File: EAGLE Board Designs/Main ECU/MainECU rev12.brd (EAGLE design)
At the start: 127 x 152.4 mm, 210 parts, among them J1 CONNECTOR-40__, J2 ADIS16460, J3 CONNECTOR-40__, J4 CONNECTOR-40__, J5 CONNECTOR-40__, K1 RELAY_DPDT_RT424024, K10 RELAY_DPDT_RT424024, K11 RELAY_DPDT_RT424024, K12 RELAY_DPDT_RT424024, K9 RELAY_DPDT_RT424024, Q3 TRANSISTOR_P_MOS_SOT-23_DMP30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, Q4 TRANSISTOR_N_MOS__DMG3406L-7, Q5 TRANSISTOR_P_MOS_SOT-23_DMP30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, Q6 TRANSISTOR_N_MOS__DMG3406L-7, U1 VOLTAGE_REGULATOR_SOT-223_3.3V, U2 TCAN1051HQV-Q1, U23 ADC128S022, U3 TCAN1051HQV-Q1, U32 ADC128S022, U33 TCAN1051HQV-Q1, U34 OPAMP_1_CHANNEL_OPA991, U37 OPAMP_1_CHANNEL_OPA991, U38 LOGICGATE_OR, U39 OPAMP_1_CHANNEL_OPA991, U4 TCAN1051HQV-Q1, U41 OPAMP_1_CHANNEL_OPA991, U42 LOGICGATE_AND_DCK3, U43 OPAMP_1_CHANNEL_OPA991, U44 LOGICGATE_NOR, U45 TCAN1051HQV-Q1, U46 TCAN1051HQV-Q1, U5 ADM8316WBX30, U6 ADC128S022, U7 ADC128S022

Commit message: ripup
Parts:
- moved A1 59.1 mm to (81.0, 175.5)
- moved C2 59.1 mm to (87.9, 176.3)
- moved C1 59.1 mm to (74.2, 174.5)
- moved TP2 59.1 mm to (83.6, 169.2)
- moved R65 50.7 mm to (-24.4, 40.9)
- moved U44 50.7 mm to (-24.4, 43.2)
- moved D37 50.7 mm to (-16.5, 40.4)
- moved D38 50.7 mm to (-20.6, 40.4)
- moved Q3 50.7 mm to (-12.4, 40.4)
- moved Q4 50.7 mm to (-20.6, 44.2)
- moved R64 50.7 mm to (-16.5, 43.2)
- moved R66 50.7 mm to (-16.5, 45.0)
- moved C26 47.3 mm to (60.5, 160.0)
- moved VR1 45.6 mm to (-14.5, 86.6)
- moved TP4 44.9 mm to (-14.0, 3.30)
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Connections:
- net +24V: no longer J1.15, J1.16
- net +5V: no longer J1.14
- net CANH_1: now also J1.16; no longer J1.12
- net CANH_2: now also J1.12; no longer J1.8
- net CANH_3: now also J1.8; no longer J1.4
- net CANL_1: now also J1.14; no longer J1.10
- net CANL_2: now also J1.10; no longer J1.6
- net CANL_3: now also J1.6; no longer J1.2
- net GND: now also J1.15, J1.4; no longer J1.1
- net SHDN_B: now also J1.1, J1.2
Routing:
- net +24V: track 250.0 -> 145.3 mm, vias 12 -> 8
- net BRAKE_HIGH: track 167.7 -> 75.3 mm, vias 2 -> 1
- net BRAKE_MISSING: track 55.5 -> 0.00 mm, vias 2 -> 0
- net CURRENT_HIGH: track 32.4 -> 1.02 mm, vias 3 -> 0
- net CURRENT: track 43.6 -> 16.0 mm
- net +5V: track 123.1 -> 98.1 mm, vias 23 -> 13
- net CURRENT_MISSING: track 17.2 -> 0.00 mm
- net BRAKE_1: track 34.9 -> 17.8 mm
- net BSPD_FAULT: track 12.9 -> 0.00 mm
- net CANH_3: track 168.7 -> 159.8 mm
- net CANH_2: track 203.2 -> 194.4 mm
- net CANL_3: track 166.0 -> 157.1 mm
- net CANH_1: track 191.1 -> 182.3 mm
- net CANL_1: track 188.2 -> 179.4 mm
- net CANL_2: track 200.2 -> 191.4 mm
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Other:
- board text added: "HyTech Racing 2023 Main ECU rev12 Designed by Mikhail Allen"
- board text removed: "HyTech Racing 2023 Main ECU rev11 Designed by Mikhail Allen"

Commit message: routing progress
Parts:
- moved TP2 42.2 mm to (74.4, 128.0)
- moved A1 42.0 mm to (70.6, 134.9)
- moved C1 38.8 mm to (63.8, 137.2), turned to 90 degrees
- moved C2 37.3 mm to (73.9, 141.7), turned to 0 degrees
- moved C26 36.0 mm to (64.5, 124.2)
- moved U$5 26.6 mm to (12.4, 125.2)
- moved BMS 21.0 mm to (46.7, 122.4)
- moved IMD 21.0 mm to (50.5, 122.4)
- moved LATCH 21.0 mm to (54.4, 122.4)
- moved R30 21.0 mm to (46.7, 120.4)
- moved R23 21.0 mm to (54.4, 120.4)
- moved R29 21.0 mm to (50.5, 120.4)
- moved D1 4.07 mm to (46.7, 141.0)
- moved D2 4.07 mm to (50.8, 141.0)
- moved D3 4.07 mm to (54.9, 141.0)
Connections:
- net +24V: now also J3.40
- net +5V: now also J3.38
- net CANH_1: now also J1.12; no longer J1.16
- net CANH_2: now also J1.8; no longer J1.12
- net CANH_3: now also J1.4; no longer J1.8
- net CANL_1: now also J1.10; no longer J1.14
- net CANL_2: now also J1.6; no longer J1.10
- net CANL_3: now also J1.2; no longer J1.6
- net GND: now also J1.1, J1.14; no longer J1.15, J1.4
- net SHDN_B: now also J1.15, J1.16; no longer J1.1, J1.2, J3.1, J3.2
- net SHDN_G: now also J3.1, J3.2; no longer J3.39, J3.40
- net STEERING_1_EXT: now also J1.25
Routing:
- net SHDN_B: track 260.1 -> 137.6 mm, vias 8 -> 7
- net STEERING_1_EXT: track 0.00 -> 108.5 mm
- net +3V3: track 475.9 -> 438.5 mm, vias 19 -> 17
- net !AD2_CS: track 97.0 -> 67.5 mm
- net +24V: track 145.3 -> 168.4 mm
- net BMS_OK: track 151.7 -> 128.8 mm, vias 3 -> 2
- net OKHS_IN: track 151.2 -> 129.1 mm
- net LATCH_BTN: track 64.9 -> 44.4 mm
- net GND: track 9.01 -> 0.00 mm, vias 39 -> 49
- net BRAKE_1: track 17.8 -> 9.07 mm
- net +5V: track 98.1 -> 104.8 mm
- net ECU_CLK: track 197.8 -> 191.4 mm
- net ECU_SDI: track 201.8 -> 195.7 mm
- net ECU_SDO: track 188.2 -> 182.9 mm
- net CANL_1: track 179.4 -> 176.1 mm
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
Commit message: routing
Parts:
- removed A: LED_0603_BLUE, HyTechDevices:0603-LED
- removed BRAKE: LED_0603_YELLOW, HyTechDevices:0603-LED
- added B_HI, B_MIS, C_HI, C_MIS: LED_0603_YELLOW, HyTechDevices:0603-LED
- added G: LED_0603_RED, HyTechDevices:0603-LED
- added R37, R54, R55: RESISTOR_0603_180, HyTechDevices:0603-RES
- B: value LED_0603_GREEN -> LED_0603_BLUE
- C: value LED_0603_YELLOW -> LED_0603_GREEN
- D: value LED_0603_ORANGE -> LED_0603_YELLOW
- E: value LED_0603_RED -> LED_0603_ORANGE
- R41, R59: value RESISTOR_0603_41.2K -> RESISTOR_0603_43K
- moved D8 148.6 mm to (109.0, 93.0), turned to 180 degrees
- moved R35 148.4 mm to (105.4, 93.0)
- moved R36 148.2 mm to (102.1, 93.0)
- moved TP3 68.6 mm to (-16.3, 115.3)
- moved C3 68.6 mm to (-22.4, 110.7)
- moved C4 68.6 mm to (-19.3, 102.6)
- moved U1 68.6 mm to (-17.5, 108.5)
- moved C93 50.5 mm to (26.4, 36.1)
- moved R60 50.5 mm to (26.4, 31.5)
- moved R61 50.5 mm to (26.4, 29.7)
- moved U37 50.5 mm to (26.4, 33.8)
- moved C92 50.3 mm to (22.1, 36.1)
- moved R59 50.3 mm to (22.1, 31.5)
- moved U34 50.3 mm to (22.1, 33.8)
- moved D43 47.8 mm to (98.6, 93.0), flipped to the top, turned to 180 degrees
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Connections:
- removed net SHDN_A: R24.1
- new net N$28: B_MIS.2, R37.2
- new net N$29: C_HI.2, R54.2
- new net N$30: C_MIS.2, R55.2
- new net TCU_RX6: A3.D25, J3.23
- new net TCU_RX7: A3.D28, J3.24
- new net TCU_TX6: A3.D24, J3.22
- new net TCU_TX7: A3.D29, J3.25
- net !STEERING_2_CS: now also A2.D9, J3.12; no longer A2.D10
- net BMS_OK: now also J3.34
- net BRAKELIGHT_EN: now also J3.9
- net BRAKE_MISSING: now also R37.1
- net CURRENT_HIGH: now also R54.1
- net CURRENT_MISSING: now also R55.1
- net ECU_CLK: now also J3.13
- net ECU_SDI: now also J3.14
- net ECU_SDO: now also J3.15
- net FL_INTERLOCK_SENSE_EXT: now also J3.30
- net FR_INTERLOCK_SENSE_EXT: now also J3.28
- net GND: now also B_HI.1, B_MIS.1, C_HI.1, C_MIS.1, G.1, J3.16, J3.17, J3.26, J3.27, J3.35, J3.36, J3.37, J3.39, J3.7, J3.8; no longer A.1, BRAKE.1
- net INERTIA_SENSE_EXT: now also J3.31
- net INVERTER_24V_EN: now also J3.10
- net INVERTER_EN: now also J3.11
- net N$13: now also G.2; no longer F.2
- net N$16: now also B.2; no longer A.2
- net N$17: now also C.2; no longer B.2
- net N$18: now also D.2; no longer C.2
- net N$19: now also E.2; no longer D.2
- net N$20: now also F.2; no longer E.2
- net N$56: now also B_HI.2; no longer BRAKE.2
- net OKHS_IN: now also J3.33
- net RL_INTERLOCK_SENSE_EXT: now also J3.32
- net RR_INTERLOCK_SENSE_EXT: now also J3.29
- net SHDN_B: now also R24.1; no longer R25.1
- net SHDN_C: now also R25.1; no longer R26.1
- net SHDN_D: now also R26.1; no longer R27.1
- net SHDN_E: now also R27.1; no longer R28.1
- net SHDN_F: now also R28.1; no longer R38.1
- net SHDN_F_READ: now also A2.D18
- net SHDN_G: now also R38.1
- net SHDN_G_READ: now also A2.D19
- net TCU_RX4: now also J3.21
- net TCU_RX5: now also J3.18
- net TCU_TX4: now also J3.20
- net TCU_TX5: now also J3.19
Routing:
- net +3V3: track 438.5 -> 237.1 mm, vias 17 -> 7
- net TCU_TX7: track 0.00 -> 104.1 mm
- net TCU_RX7: track 0.00 -> 100.4 mm
- net TCU_RX6: track 0.00 -> 96.5 mm
- net BSPD_OK: track 155.0 -> 59.8 mm, vias 2 -> 0
- net TCU_TX6: track 0.00 -> 93.8 mm
- net +24V: track 168.4 -> 259.5 mm, vias 8 -> 9
- net BRAKE_HIGH: track 75.3 -> 0.00 mm, vias 1 -> 0
- net SHDN_A: track 63.8 -> 0.00 mm, vias 7 -> 0
- net !STEERING_2_CS: track 0.00 -> 38.9 mm, vias 0 -> 1
- net SHDN_B: track 137.6 -> 173.6 mm, vias 7 -> 8
- net FR_INTERLOCK_SENSE: track 39.9 -> 5.41 mm, vias 1 -> 0
- net INERTIA_SENSE_EXT: track 0.70 -> 33.4 mm
- net SHDN_F_READ: track 38.1 -> 6.14 mm, vias 1 -> 0
- net RR_INTERLOCK_SENSE: track 37.0 -> 5.25 mm, vias 1 -> 0
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
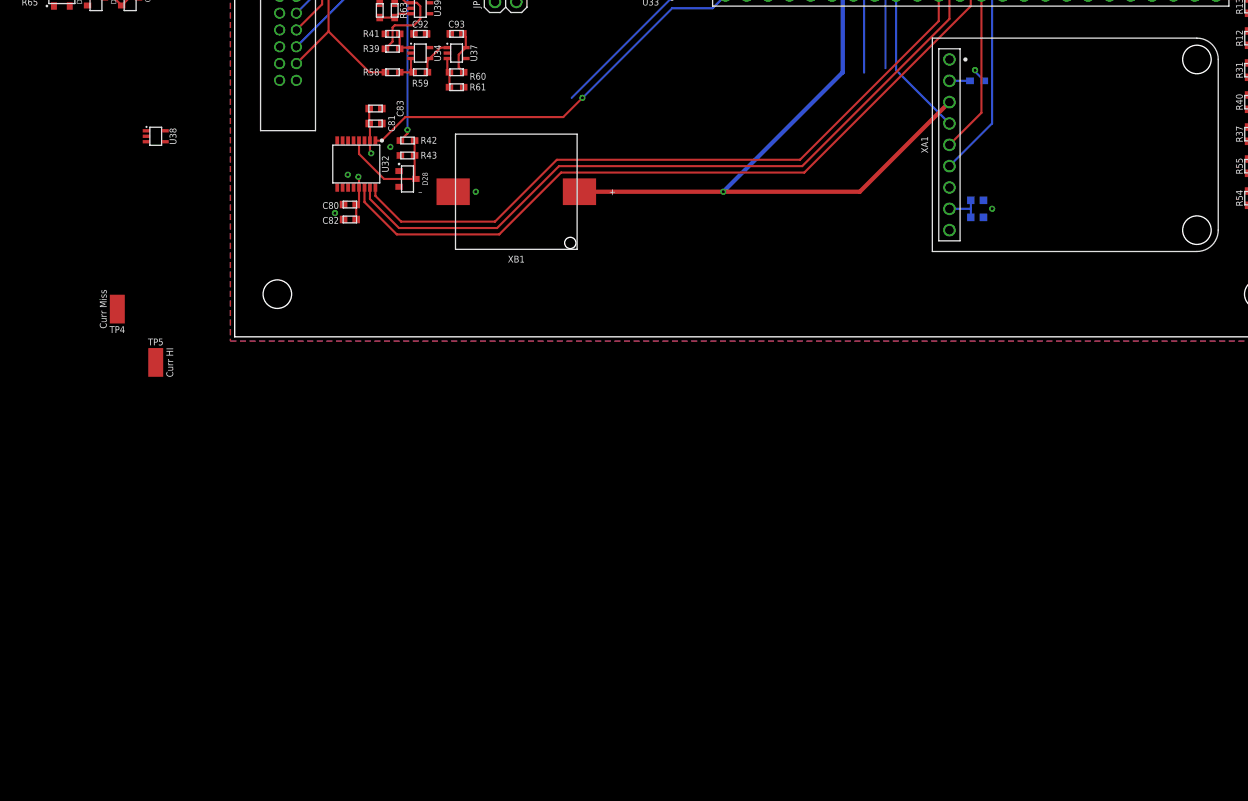
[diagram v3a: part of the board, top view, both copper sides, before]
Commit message: added nrf/esp board to schematic
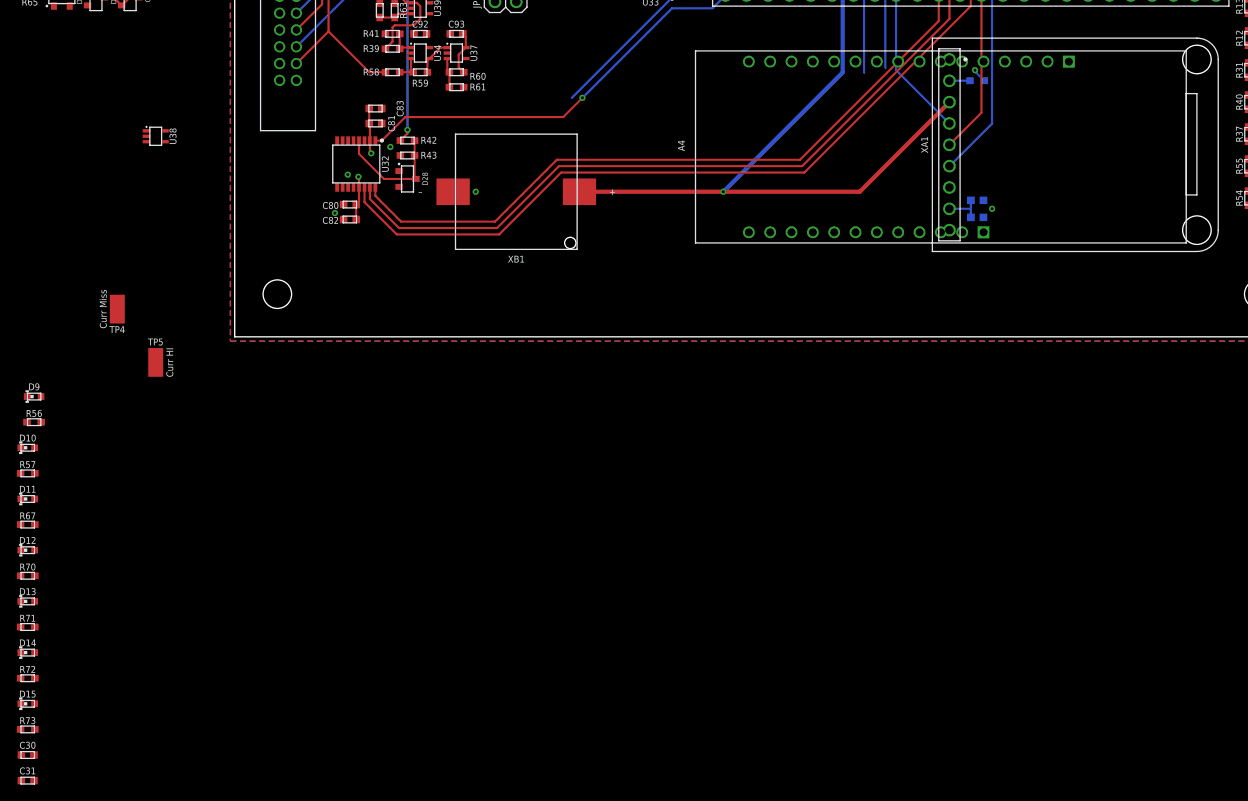
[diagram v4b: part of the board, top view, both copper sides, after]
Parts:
- added A4: NRF9160LTE, HyTechDevices:NRF9160LTE
- added C30: CAPACITOR_0603_10V_0.1UF, HyTechDevices:0603-CAP
- added C31: CAPACITOR_0603_10V_1UF, HyTechDevices:0603-CAP
- added D10, D11, D12, D13, D14, D15, D9: LED_0603_RED, HyTechDevices:0603-LED
- added R56, R57, R67, R70, R71, R72, R73: RESISTOR_0603_2K, HyTechDevices:0603-RES
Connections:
- removed net XBDI: A3.D8
- removed net XBDO: A3.D7
- new net ESP_OK: A4.7, R57.1
- new net ESP_OTHER_1: A4.6
- new net ESP_OTHER_2: A4.8
- new net ESP_RX: A3.D35, A4.TX
- new net ESP_TX: A3.D34, A4.RX
- new net GPS_OK: A4.4, R71.1
- new net GPS_RTK_OK: A4.5, R72.1
- new net N$31: D9.2, R56.2
- new net N$32: D10.2, R57.2
- new net N$35: D11.2, R67.2
- new net N$36: D12.2, R70.2
- new net N$37: D13.2, R71.2
- new net N$38: D14.2, R72.2
- new net N$39: D15.2, R73.2
- new net NRF_LTE_OK: A4.2, R56.1, R67.1, R73.1
- new net NRF_MQTT_OK: A4.3, R70.1
- new net NRF_RX: A3.D7, A4.A4
- new net NRF_TX: A3.D8, A4.A5
- net +5V: now also A4.VUSB, C30.1, C31.1
- net 3V3: now also A4.3V3
- net GND: now also A4.GND, C30.2, C31.2, D10.1, D11.1, D12.1, D13.1, D14.1, D15.1, D9.1
- net VBAT: now also A4.VBAT
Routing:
- net XBDO: track 42.9 -> 0.00 mm, vias 1 -> 0
- net NRF_RX: track 0.00 -> 42.9 mm, vias 0 -> 1
- net XBDI: track 37.9 -> 0.00 mm, vias 1 -> 0
- net NRF_TX: track 0.00 -> 37.9 mm, vias 0 -> 1

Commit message: remove ult gps. merged filter board. routing
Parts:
- removed C78: CAPACITOR_0603_10V_0.1UF, HyTechDevices:0603-CAP
- removed C79: CAPACITOR_0603_10V_1UF, HyTechDevices:0603-CAP
- removed J4, J5: CONNECTOR-40__, HyTechDevices:EHT-120-01
- removed R14: RESISTOR_0603_10K, HyTechDevices:0603-RES
- removed XA1: ULTIMATE_GPS, HyTechDevices:ULTIMATE_GPS
- added C105, C106, C107, C108, C109, C110, C111, C112, C113, C114, C115, C36, C38, C44, C46, C52, C58, C64, C66, C72, C74, C88, C91, C94, C96, C97, C98: CAPACITOR_0603_10V_680PF, HyTechDevices:0603-CAP
- added C32, C33, C34, C35, C37, C39, C41, C43, C45, C47, C49, C51, C53, C59, C61, C63, C65, C67, C69, C71, C73, C75, C77, C87, C89: CAPACITOR_0603_10V_0.1UF, HyTechDevices:0603-CAP
- added C40, C42, C48, C50, C60, C62, C68, C70, C76, C86, C90: CAPACITOR_0603_10V_1UF, HyTechDevices:0603-CAP
- added R100, R103, R104, R107, R108, R111, R112, R115, R116, R119, R120, R123, R124, R127, R128, R98: RESISTOR_0603_10K, HyTechDevices:0603-RES
- added R101, R105, R109, R113, R117, R121, R125, R80, R82, R84, R86, R88, R90, R94: RESISTOR_0603_13K, HyTechDevices:0603-RES
- added R102, R106, R110, R114, R118, R122, R126, R81, R83, R85, R87, R89, R91, R96: RESISTOR_0603_3.3K, HyTechDevices:0603-RES
- added R74, R76, R78: RESISTOR_0603_1.13K, HyTechDevices:0603-RES
- added R75, R77, R79: RESISTOR_0603_10.2K, HyTechDevices:0603-RES
- added R92, R93, R95, R97, R99: RESISTOR_0603_100K, HyTechDevices:0603-RES
- added TP1, TP7, TP8: TEST_POINT, HyTechDevices:5015
- added U10, U8, U9: OPAMP_1_CHANNEL_OPA991, HyTechDevices:SC-70-5
- added U11, U12, U13: LOGICGATE_OR, HyTechDevices:SC-70-5
- added U14, U15, U16, U17, U18, U19, U20, U21, U22, U24, U25: MAX7400, HyTechDevices:SOIC-08(NARROW,0.15")
- moved R69 118.2 mm to (-90.7, 44.5), turned to 180 degrees
- moved R68 116.2 mm to (-90.7, 46.0), turned to 0 degrees
- moved U39 114.2 mm to (-90.7, 57.1)
- moved U43 113.5 mm to (-90.7, 48.0), turned to 270 degrees
- moved C95 111.9 mm to (-88.6, 57.4), flipped to the bottom, turned to 270 degrees
- moved R63 111.7 mm to (-90.9, 58.2), flipped to the bottom, turned to 180 degrees
- moved R62 109.7 mm to (-90.9, 56.6), flipped to the bottom, turned to 0 degrees
- moved 3V3 106.6 mm to (32.5, -21.3)
- moved 5V0 106.6 mm to (32.5, -17.5)
- moved BSPD 106.6 mm to (32.5, -25.1)
- moved B_HI 106.6 mm to (32.5, -29.0)
- moved B_MIS 106.6 mm to (32.5, -32.8)
- moved C_HI 106.6 mm to (32.5, -40.4)
- moved C_MIS 106.6 mm to (32.5, -36.6)
- moved R12 106.6 mm to (30.5, -21.3)
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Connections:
- removed net N$52: R14.1, XA1.EN
- new net CURRENT_OOR: U11.4, U12.1
- new net CURRENT_OOR_HI: TP1.1, U11.1, U8.4
- new net CURRENT_OOR_LO: TP4.1, U11.2, U39.4
- new net N$100: C108.1, R115.1, R116.2
- new net N$101: R117.2, R118.2, R119.2
- new net N$102: C110.1, R119.1, R120.2
- new net N$103: R121.2, R122.2, R123.2
- new net N$104: C112.1, R123.1, R124.2
- new net N$105: R125.2, R126.2, R127.2
- new net N$106: C114.1, R127.1, R128.2
- new net N$33: R62.2, R63.1, U39.1
- new net N$34: R74.1, R75.2, U8.3
- new net N$46: R76.2, R77.1, U9.1
- new net N$48: R78.1, R79.2, U10.3
- new net N$49: R80.1, R81.2, U14.2
- new net N$50: C35.1, U14.1, U14.6
- new net N$51: C36.1, U14.8
- new net N$53: R82.1, R83.2, U15.2
- new net N$54: C37.1, U15.1, U15.6
- new net N$55: C38.1, U15.8
- new net N$57: R84.1, R85.2, U16.2
- new net N$63: C43.1, U16.1, U16.6
- new net N$64: C44.1, U16.8
- new net N$66: R86.1, R87.2, U17.2
- new net N$69: C45.1, U17.1, U17.6
- new net N$70: C46.1, U17.8
- new net N$71: R88.1, R89.2, U18.2
- new net N$77: C52.1, U18.8
- new net N$78: R90.1, R91.2, U19.2
- new net N$79: C53.1, U19.1, U19.6
- new net N$80: C58.1, U19.8
- new net N$81: C87.1, U25.1, U25.6
- new net N$82: C63.1, U20.1, U20.6
- new net N$83: C64.1, U20.8
- new net N$84: C88.1, U25.8
- new net N$85: C65.1, U21.1, U21.6
- new net N$86: C66.1, U21.8
- new net N$87: R101.2, R102.2, R103.2
- new net N$88: C71.1, U22.1, U22.6
- new net N$89: C72.1, U22.8
- new net N$90: R94.2, R96.2, R98.2
- new net N$91: C73.1, U24.1, U24.6
- new net N$92: C74.1, U24.8
- new net N$93: C91.1, R100.2, R98.1
- new net N$94: C96.1, R103.1, R104.2
- new net N$95: R105.2, R106.2, R107.2
- new net N$96: C98.1, R107.1, R108.2
- new net N$97: R109.2, R110.2, R111.2
- new net N$98: C106.1, R111.1, R112.2
- new net N$99: R113.2, R114.2, R115.2
- new net REFERENCE_OOR: U12.2, U13.4
- new net REFERENCE_OOR_HI: TP8.1, U10.4, U13.1
- new net REFERENCE_OOR_LO: TP7.1, U13.2, U9.4
- net +5V: now also C32.1, C33.1, C34.1, C39.1, C40.1, C41.1, C42.1, C47.1, C48.1, C49.1, C50.1, C59.1, C60.1, C61.1, C62.1, C67.1, C68.1, C69.1, C70.1, C75.1, C76.1, C77.1, C86.1, C89.1, C90.1, R63.2, R74.2, R77.2, R78.2, U10.5, U11.5, U12.5, U13.5, U14.4, U14.7, U15.4, U15.7, U16.4, U16.7, U17.4, U17.7, U18.4, U18.7, U19.4, U19.7, U20.4, U20.7, U21.4, U21.7, U22.4, U22.7, U24.4, U24.7, U25.4, U25.7, U8.5, U9.5; no longer C78.1, C79.1, J4.1, R14.2, R62.2, XA1.VIN
- net 3V3: no longer XA1.3.3V
- net ACCEL_1: now also U20.5; no longer J5.5
- net ACCEL_1_EXT: now also R93.2, U20.2; no longer J5.3
- net ACCEL_2: now also U21.5; no longer J5.9
- net ACCEL_2_EXT: now also R95.2, U21.2; no longer J5.7
- net BRAKE_1: now also U22.5; no longer J5.13
- net BRAKE_1_EXT: now also R97.2, U22.2; no longer J5.11
- net BRAKE_2: now also U24.5; no longer J5.17
- net BRAKE_2_EXT: now also R99.2, U24.2; no longer J5.15
- net BRAKE_MISSING: now also U38.2; no longer U38.1
- net BRAKE_PRESSURE_F: now also C94.1, R100.1; no longer J5.28
- net BRAKE_PRESSURE_F_EXT: now also R94.1; no longer J5.27
- net BRAKE_PRESSURE_R: now also C97.1, R104.1; no longer J5.30
- net BRAKE_PRESSURE_R_EXT: now also R101.1; no longer J5.29
- net CURRENT: now also U14.5, U39.3, U8.1; no longer J5.34, U39.1
- net CURRENT_EXT: now also R80.2; no longer J5.32
- net CURRENT_MISSING: now also U12.4, U38.1; no longer TP4.1, U38.2, U39.4
- net GND: now also C105.2, C106.2, C107.2, C108.2, C109.2, C110.2, C111.2, C112.2, C113.2, C114.2, C115.2, C32.2, C33.2, C34.2, C35.2, C36.2, C37.2, C38.2, C39.2, C40.2, C41.2, C42.2, C43.2, C44.2, C45.2, C46.2, C47.2, C48.2, C49.2, C50.2, C51.2, C52.2, C53.2, C58.2, C59.2, C60.2, C61.2, C62.2, C63.2, C64.2, C65.2, C66.2, C67.2, C68.2, C69.2, C70.2, C71.2, C72.2, C73.2, C74.2, C75.2, C76.2, C77.2, C86.2, C87.2, C88.2, C89.2, C90.2, C91.2, C94.2, C96.2, C97.2, C98.2, R102.1, R106.1, R110.1, R114.1, R118.1, R122.1, R126.1, R62.1, R75.1, R76.1, R79.1, R81.1, R83.1, R85.1, R87.1, R89.1, R91.1, R92.1, R93.1, R95.1, R96.1, R97.1, R99.1, U10.2, U11.3, U12.3, U13.3, U14.3, U15.3, U16.3, U17.3, U18.3, U19.3, U20.3, U21.3, U22.3, U24.3, U25.3, U8.2, U9.2; no longer C78.2, C79.2, J4.10, J4.12, J4.14, J4.16, J4.18, J4.2, J4.20, J4.22, J4.24, J4.26, J4.28, J4.30, J4.32, J4.34, J4.36, J4.38, J4.4, J4.6, J4.8, J5.10, J5.12, J5.14, J5.16, J5.18, J5.2, J5.20, J5.22, J5.24, J5.26, J5.31, J5.33, J5.35, J5.37, J5.4, J5.6, J5.8, R63.1, XA1.GND
- net GPS_FIX: no longer XA1.FIX
- net GPS_RX: no longer XA1.RX
- net GPS_TX: no longer XA1.TX
- net LOAD_FL: now also U16.5; no longer J4.5
- net LOAD_FL_EXT: now also R84.2; no longer J4.3
- net LOAD_FR: now also U17.5; no longer J4.9
- net LOAD_FR_EXT: now also R86.2; no longer J4.7
- net LOAD_RL: no longer J4.13
- net LOAD_RL_EXT: now also R88.2; no longer J4.11
- net LOAD_RR: now also U18.5, U19.5; no longer J4.17
- net LOAD_RR_EXT: now also R90.2; no longer J4.15
- net N$72: now also C51.1, U18.1, U18.6; no longer R62.1, R63.2, U39.3
- net REFERENCE: now also U10.1, U15.5, U9.3; no longer J5.38
- net REFERENCE_EXT: now also R82.2; no longer J5.36
- net SPN_POT_1: now also C105.1, R108.1; no longer J4.21
- net SPN_POT_1_EXT: now also R105.1; no longer J4.19
- net SPN_POT_2: now also C107.1, R112.1; no longer J4.25
- net SPN_POT_2_EXT: now also R109.1; no longer J4.23
- net SPN_POT_3: now also C109.1, R116.1; no longer J4.29
- net SPN_POT_3_EXT: now also R113.1; no longer J4.27
- net SPN_POT_4: now also C111.1, R120.1; no longer J4.33
- net SPN_POT_4_EXT: now also R117.1; no longer J4.31
- net SPN_POT_5: now also C113.1, R124.1; no longer J4.37
- net SPN_POT_5_EXT: now also R121.1; no longer J4.35
- net SPN_POT_6: now also C115.1, R128.1; no longer J5.1
- net SPN_POT_6_EXT: now also R125.1; no longer J4.39
- net STEERING_1: now also U25.5; no longer J5.21
- net STEERING_1_EXT: now also R92.2, U25.2; no longer J5.19
- net VBAT: no longer XA1.VBAT
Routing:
- net REFERENCE_EXT: track 123.1 -> 0.00 mm
- net CURRENT_EXT: track 121.1 -> 0.00 mm
- net BRAKE_PRESSURE_R_EXT: track 117.3 -> 0.00 mm
- net BRAKE_PRESSURE_F_EXT: track 117.3 -> 0.00 mm
- net STEERING_1_EXT: track 108.5 -> 0.00 mm
- net TELEM_SDO: track 103.8 -> 0.00 mm, vias 1 -> 0
- net BRAKE_2_EXT: track 101.6 -> 0.00 mm
- net TELEM_SDI: track 100.7 -> 0.00 mm, vias 1 -> 0
- net BRAKE_1_EXT: track 99.6 -> 0.00 mm
- net ACCEL_2_EXT: track 92.9 -> 0.00 mm
- net ACCEL_1_EXT: track 90.9 -> 0.00 mm
- net VBAT: track 90.9 -> 1.80 mm, vias 1 -> 0
- net TELEM_CLK: track 82.3 -> 0.00 mm
- net ECU_SDO: track 203.0 -> 122.5 mm, vias 6 -> 3
- net ECU_SDI: track 211.6 -> 131.8 mm, vias 8 -> 5
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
